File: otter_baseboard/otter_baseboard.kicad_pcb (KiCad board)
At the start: 4 copper layers, 139.7 x 35.6 mm, 25 parts, among them J1 Conn_02x20_Odd_Even, J2 Conn_02x08_Odd_Even, J3 Conn_02x08_Odd_Even, J4 Conn_02x08_Odd_Even, J5 Conn_02x08_Odd_Even, J6 Conn_02x08_Odd_Even, J7 Conn_02x20_Odd_Even

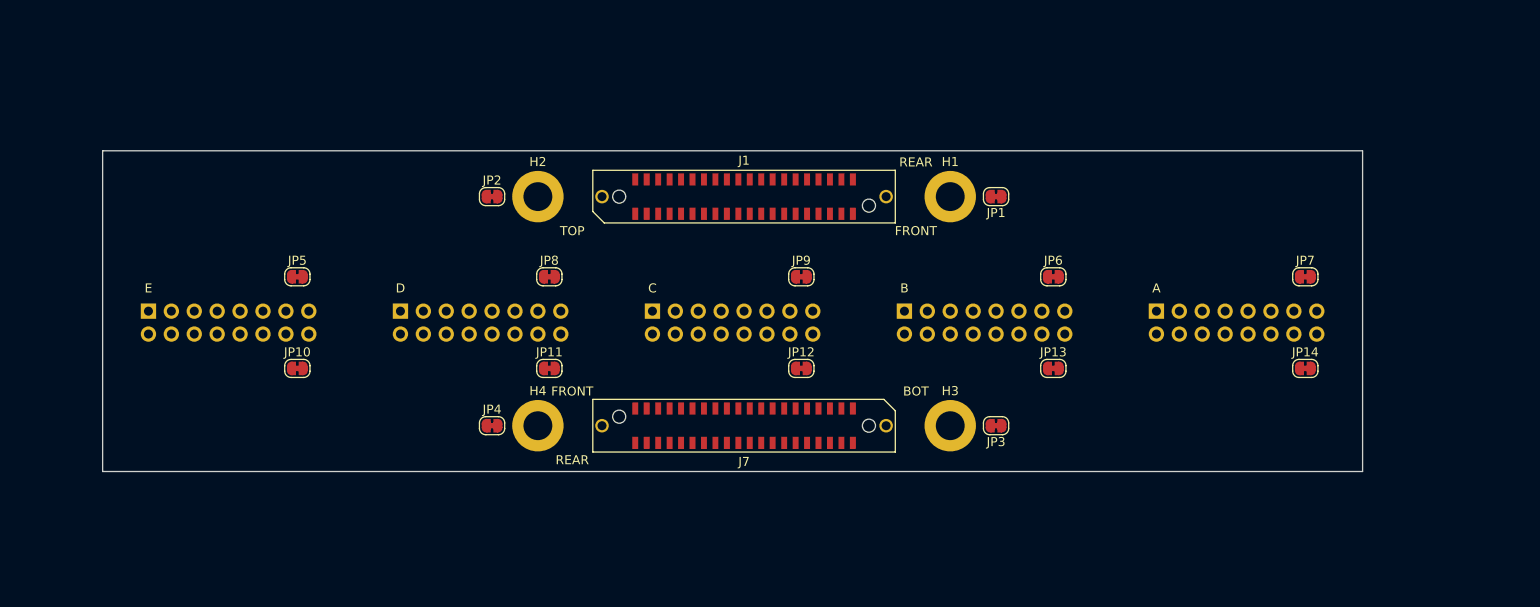
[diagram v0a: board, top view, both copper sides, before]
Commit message: baseboard routed
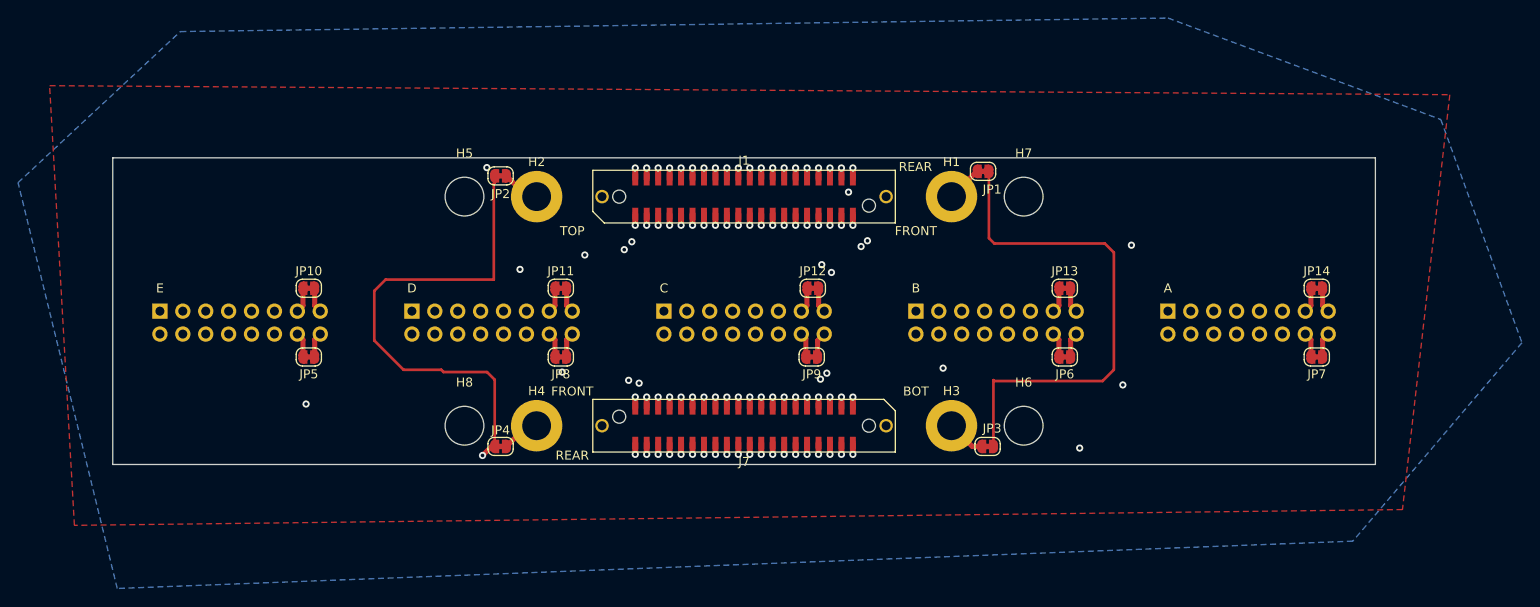
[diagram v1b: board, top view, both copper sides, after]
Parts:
- added H5: MountingHole, MountingHole:MountingHole_4.3mm_M4_ISO7380, F.Cu at (-31.0, -12.7)
- added H6: MountingHole, MountingHole:MountingHole_4.3mm_M4_ISO7380, F.Cu at (31.0, 12.7)
- added H7: MountingHole, MountingHole:MountingHole_4.3mm_M4_ISO7380, F.Cu at (31.0, -12.7)
- added H8: MountingHole, MountingHole:MountingHole_4.3mm_M4_ISO7380, F.Cu at (-31.0, 12.7)
- J1, J7: footprint Connector_PCBEdge:Samtec_MECF-20-01-NP-L-DV-WT_2x20_P1.27mm_Socket_Horizontal -> custom_footprints:Samtec_MECF-20-01-NP-L-DV-WT_2x20_P1.27mm_Socket_Horizontal_mod
- moved JP10 8.98 mm to (-48.3, -2.54)
- moved JP11 8.98 mm to (-20.3, -2.54)
- moved JP12 8.98 mm to (7.62, -2.54)
- moved JP13 8.98 mm to (35.6, -2.54)
- moved JP14 8.98 mm to (63.5, -2.54)
- moved JP5 8.98 mm to (-48.3, 5.08)
- moved JP6 8.98 mm to (35.6, 5.08)
- moved JP7 8.98 mm to (63.5, 5.08)
- moved JP8 8.98 mm to (-20.3, 5.08)
- moved JP9 8.96 mm to (7.50, 5.08)
- moved JP1 3.15 mm to (26.5, -15.5)
- moved JP2 2.48 mm to (-27.0, -15.0)
- moved JP3 2.48 mm to (27.0, 15.0)
- moved JP4 2.48 mm to (-27.0, 15.0)
- moved J2 1.27 mm to (-64.8, 0.00)
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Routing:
- net GND: track 0.00 -> 111.3 mm, vias 0 -> 1
- net /E3T: track 0.00 -> 76.6 mm, vias 0 -> 1
- net /A7B: track 0.00 -> 75.2 mm, vias 0 -> 1
- net /E4T: track 0.00 -> 71.5 mm, vias 0 -> 1
- net /A10B: track 0.00 -> 67.6 mm, vias 0 -> 1
- net /E4B: track 0.00 -> 66.8 mm, vias 0 -> 1
- net /E7T: track 0.00 -> 65.3 mm, vias 0 -> 1
- net /E2B: track 0.00 -> 64.9 mm, vias 0 -> 1
- net /A9B: track 0.00 -> 64.8 mm, vias 0 -> 1
- net /A2T: track 0.00 -> 64.7 mm, vias 0 -> 1
- net /E1B: track 0.00 -> 64.6 mm, vias 0 -> 1
- net /A10T: track 0.00 -> 63.6 mm, vias 0 -> 2
- net /E3B: track 0.00 -> 63.5 mm, vias 0 -> 1
- net /E6T: track 0.00 -> 62.0 mm, vias 0 -> 1
- net /A1T: track 0.00 -> 61.1 mm, vias 0 -> 1
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- added copper zone on B.Cu, net GND
- added copper zone on F.Cu, net GND
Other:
- board size 139.7 x 35.6 mm -> 140 x 34 mm
- net class Default: clearance 0.2 -> 0.15
- rule trace_clearance: 0.2 -> 0.15

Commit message: fix baseboard connector position
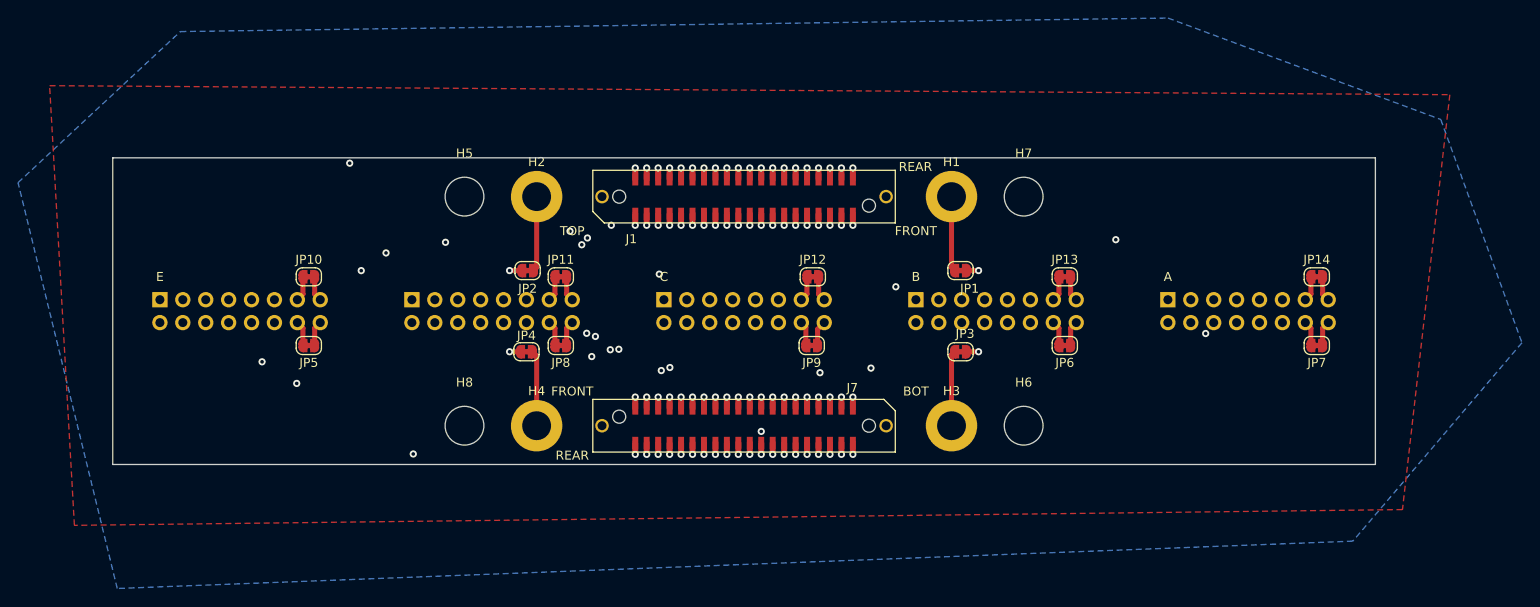
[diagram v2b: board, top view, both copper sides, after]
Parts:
- moved JP1 11.3 mm to (24.0, -4.50)
- moved JP2 10.9 mm to (-24.0, -4.50)
- moved JP3 10.9 mm to (24.0, 4.50)
- moved JP4 10.9 mm to (-24.1, 4.50)
- moved J2 1.27 mm to (-64.8, -1.27)
- moved J3 1.27 mm to (-36.8, -1.27)
- moved J4 1.27 mm to (-8.89, -1.27)
- moved J5 1.27 mm to (19.1, -1.27)
- moved J6 1.27 mm to (47.0, -1.27)
- moved JP10 1.27 mm to (-48.3, -3.81)
- moved JP11 1.27 mm to (-20.3, -3.81)
- moved JP12 1.27 mm to (7.62, -3.81)
- moved JP13 1.27 mm to (35.6, -3.81)
- moved JP14 1.27 mm to (63.5, -3.81)
- moved JP5 1.27 mm to (-48.3, 3.81)
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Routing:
- net GND: track 111.3 -> 5.27 mm, vias 1 -> 4
- net /C9T: track 36.1 -> 69.9 mm, vias 3 -> 2
- net /D2T: track 21.4 -> 41.2 mm, vias 1 -> 2
- net /C3B: track 31.6 -> 43.7 mm
- net /A7B: track 75.2 -> 63.5 mm, vias 1 -> 2
- net /E3T: track 76.6 -> 69.1 mm
- net /C2T: track 19.7 -> 26.5 mm
- net /E10B: track 51.6 -> 57.3 mm, vias 1 -> 2
- net /B6T: track 27.2 -> 22.7 mm
- net Net-(H1-Pad1): track 4.01 -> 8.34 mm
- net /A10B: track 67.6 -> 71.8 mm
- net Net-(H4-Pad1): track 4.30 -> 8.40 mm
- net Net-(H2-Pad1): track 4.30 -> 8.34 mm
- net Net-(H3-Pad1): track 4.35 -> 8.34 mm
- net /C10T: track 37.7 -> 41.7 mm, vias 3 -> 1
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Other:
- board text removed: "D"

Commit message: enbiggen pcb dowel holes
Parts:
- H5, H6, H7, H8: footprint MountingHole:MountingHole_4.3mm_M4_ISO7380 -> MountingHole:MountingHole_6.4mm_M6
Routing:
- net /A1T: track 60.5 -> 62.5 mm
- net /A3B: track 50.7 -> 52.6 mm
- net /E1T: track 47.8 -> 49.7 mm
- net /E2B: track 65.0 -> 66.1 mm
- net /E10B: track 57.3 -> 58.5 mm
- net /E7T: track 61.8 -> 62.8 mm
- net /D4T: track 42.5 -> 41.9 mm
- net /E3T: track 69.1 -> 69.6 mm

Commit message: update silk
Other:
- board text added: "9e3598e"
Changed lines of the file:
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@@
   (general
     (thickness 1.6)
-    (drawings 24)
+    (drawings 26)
     (tracks 921)
     (zones 0)
@@
   )
   (setup
-    (last_trace_width 0.4)
+    (last_trace_width 0.25)
     (user_trace_width 0.3)
     (user_trace_width 0.4)
@@
       (outputformat 1)
       (mirror false)
-      (drillshape 1)
+      (drillshape 0)
       (scaleselection 1)
-      (outputdirectory ""))
+      (outputdirectory "output/"))
   )
   (net 0 "")
@@
     (pad 1 np_thru_hole circle (at 0 0) (size 6.4 6.4) (drill 6.4) (layers *.Cu *.Mask))
   )
+  (gr_text 9e3598e (at -66 16) (layer B.SilkS)
+    (effects (font (size 1 1) (thickness 0.15)) (justify mirror))
+  )
+  (gr_text 9e3598e (at -66 16) (layer F.SilkS)
+    (effects (font (size 1 1) (thickness 0.15)))
+  )
   (gr_text E (at -64.77 -3.81) (layer B.SilkS)

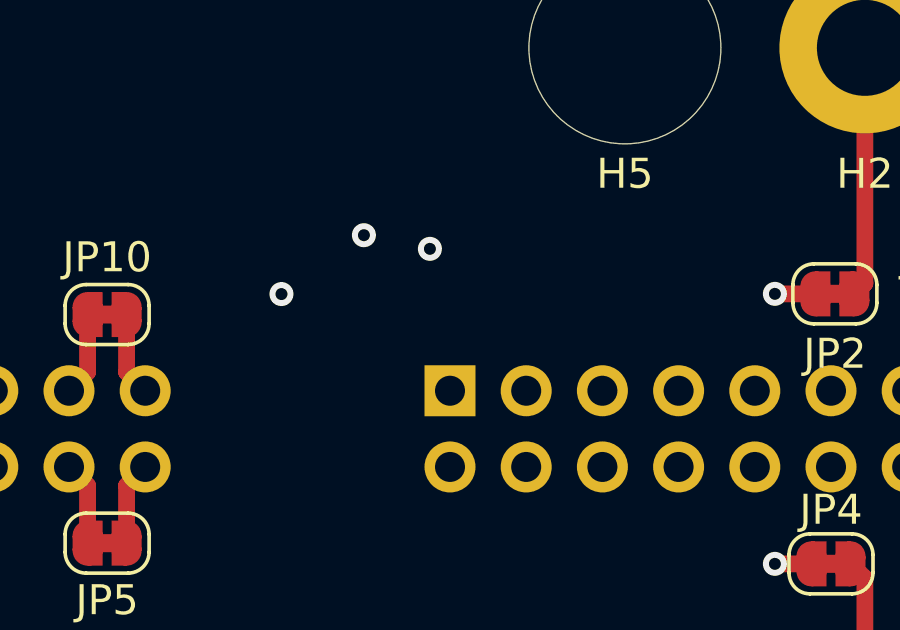
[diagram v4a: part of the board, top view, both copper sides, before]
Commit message: update pdb silk and add missing letter to otter baseboard
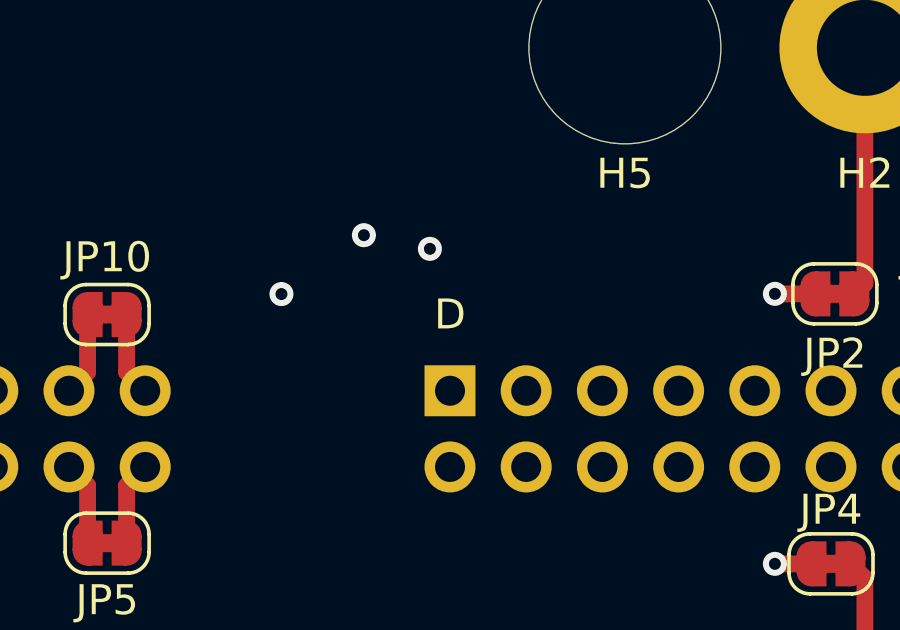
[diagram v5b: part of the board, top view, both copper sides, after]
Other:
- board text added: "D"
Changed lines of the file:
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@@
   (general
     (thickness 1.6)
-    (drawings 26)
+    (drawings 28)
     (tracks 921)
     (zones 0)
@@
     (pad 1 np_thru_hole circle (at 0 0) (size 6.4 6.4) (drill 6.4) (layers *.Cu *.Mask))
   )
+  (gr_text D (at -36.83 -3.81) (layer F.SilkS)
+    (effects (font (size 1 1) (thickness 0.15)))
+  )
+  (gr_text D (at -36.83 -3.81) (layer B.SilkS)
+    (effects (font (size 1 1) (thickness 0.15)) (justify mirror))
+  )
   (gr_text 9e3598e (at -66 16) (layer B.SilkS)

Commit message: update silk
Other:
- board text added: "609cc51"
- board text removed: "9e3598e"
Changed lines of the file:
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@@
     (effects (font (size 1 1) (thickness 0.15)) (justify mirror))
   )
-  (gr_text 9e3598e (at -66 16) (layer B.SilkS)
+  (gr_text 609cc51 (at -66 16) (layer B.SilkS)
     (effects (font (size 1 1) (thickness 0.15)) (justify mirror))
   )
-  (gr_text 9e3598e (at -66 16) (layer F.SilkS)
+  (gr_text 609cc51 (at -66 16) (layer F.SilkS)
     (effects (font (size 1 1) (thickness 0.15)))
   )
